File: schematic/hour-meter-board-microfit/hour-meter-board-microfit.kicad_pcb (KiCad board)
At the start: 2 copper layers, 80 x 92 mm, 143 parts, among them J101 VIN 9-30V, J201 USB-C, J301 DIN1 DIN2 COM, J501 WP, J701 RS485, J702 TERM, J703 BIAS, J801 UART, J802 GPS, J803 QWIIC, J804 EXP, J902 5V AIN1 GND DOUT1 GND, Q201 MMBT3904, Q202 MMBT3904, SW201 RESET, SW202 BOOT, U101 LM2596S-ADJ, U201 ESP32-WROOM-32E-N4, U202 CH340C, U203 USBLC6-2SC6, U204 AMS1117-3.3, U301 PC817C-S, U302 PC817C-S, U401 DS3231MZ+TRL, U501 AT24C256 DIP-8 (socketed), U601 MPU-6500, U602 LIS3MDLTR, U701 THVD2410DR, U801 74LVC1G17GW, U802 SRV05-4, U901 ADS1115IDGST, U902 SN74AHCT1G125DBVR, U903 BSP75N

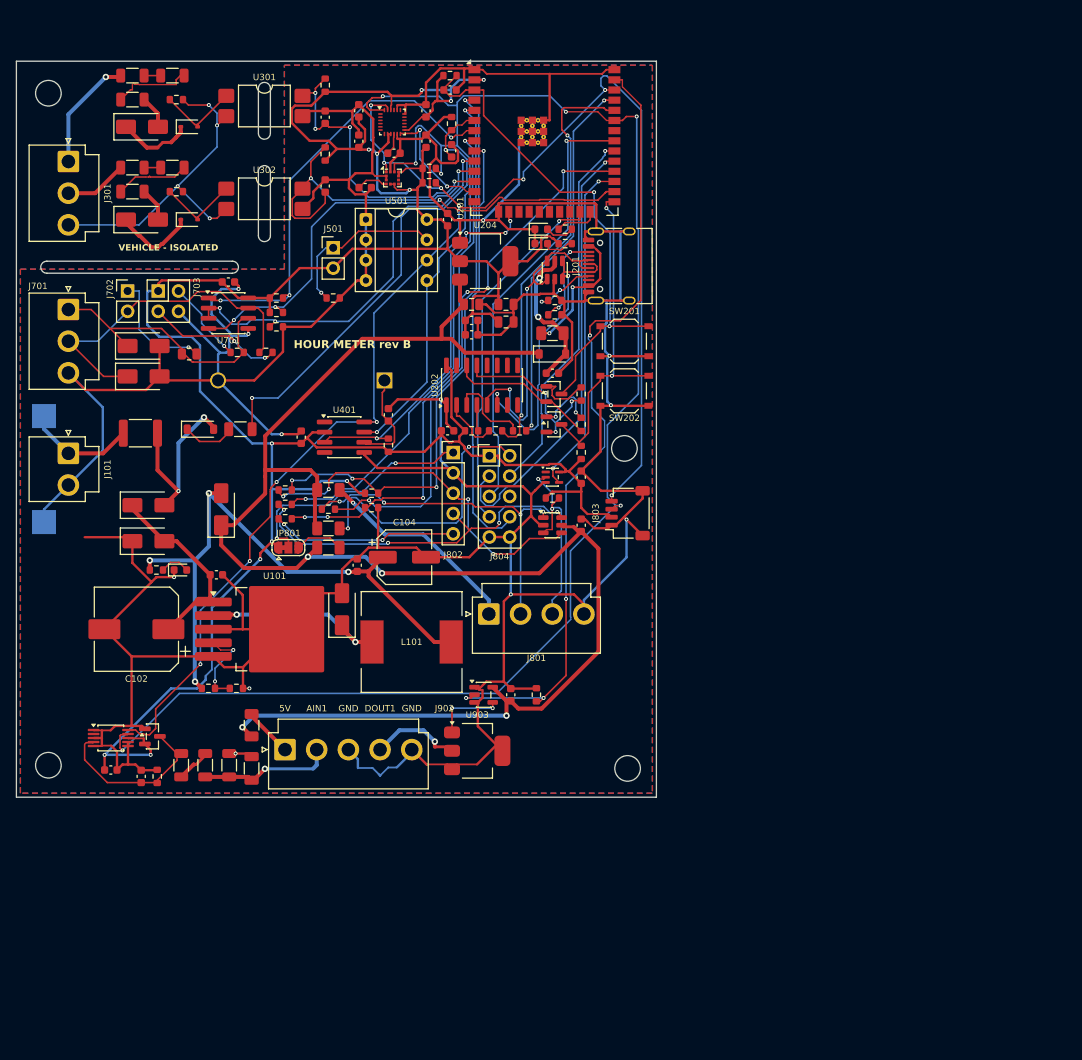
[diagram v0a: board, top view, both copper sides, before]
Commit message: feat(pcb): lay out the Micro-Fit harness board on 80 x 80 mm
- Every port on the left edge: J1 (Micro-Fit 2x7, mating face at the
  edge), the GPS JST GH port and the Qwiic port below it; USB-C and the
  buttons stay on the right edge.
- Vehicle zone beside J1: the DIN island in the top-left corner (slots,
  barrier rule areas, no pour; the GND pour keeps 3.65 mm away), then the
  RS485, UART, AIN1 and DOUT1 front ends, with the BSP75N's drain facing
  J1 so the 0.5 A loop stays at the connector. The LM2596 stage keeps
  its bottom strip; the coin cell moves to the bottom-right corner.
- The ESP32/USB block, the IMU and the LM2596 stage keep the I/O board's
  placement, and `reuse` copies their routing; KiCad's DRC drops any
  copied piece that clashes with the new layout. Freerouting routed the
  rest: DRC 0 errors, 0 unconnected, 0 parity, 2 copper layers.
- `silk` re-applies the labels on the routed board: a legend for the
  RS485 solder jumpers and the J1 pinout on the bottom silkscreen.
- J1's 3D model is JLCPCB's (C277677), fitted to the KiCad footprint.
- Order files: BOM 68 lines, CPL 125; all in stock for 10 boards.
- README: harness pinout and parts, ports, solder jumpers, enclosure.
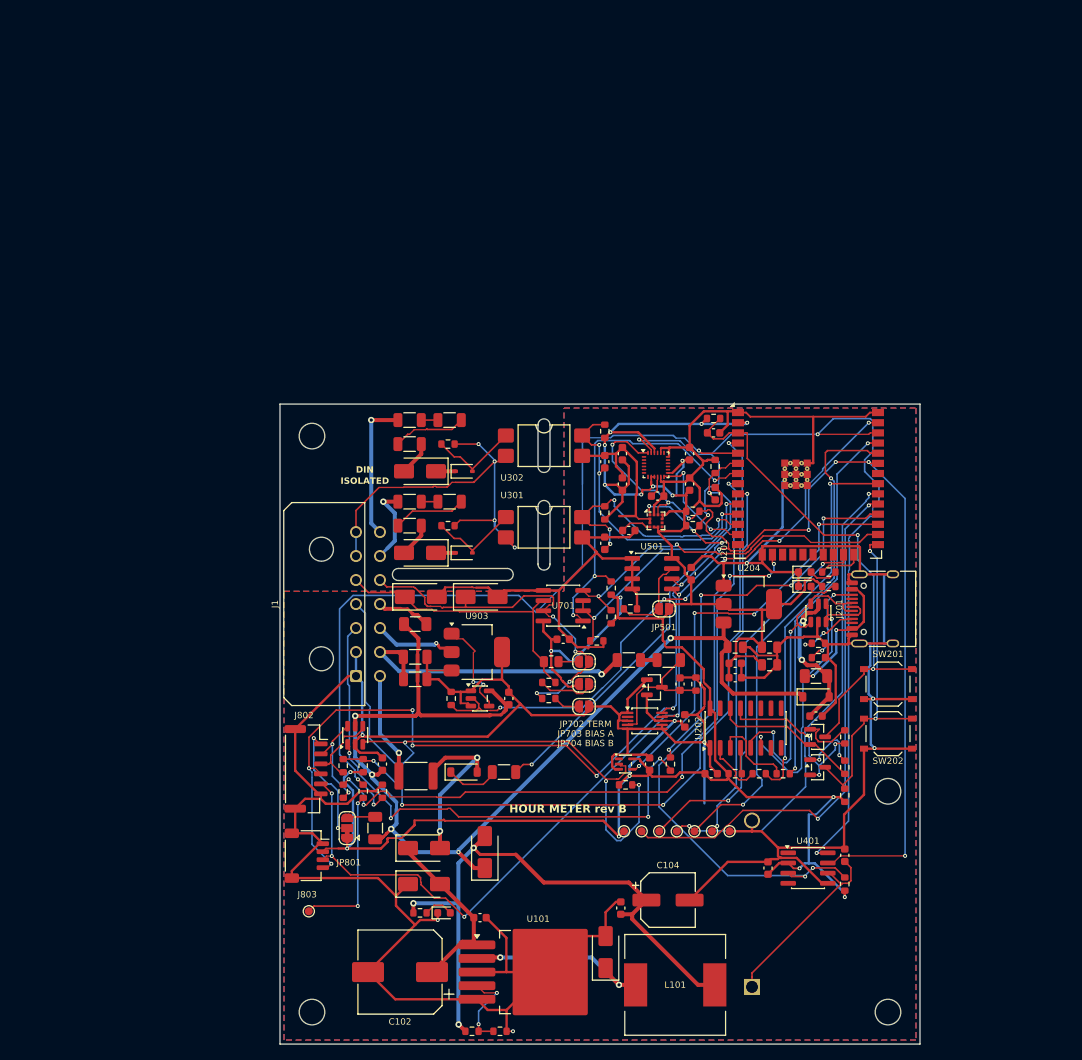
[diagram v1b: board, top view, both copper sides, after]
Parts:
- removed F802, F902: 0.2A, Fuse:Fuse_1206_3216Metric
- removed J101: VIN 9-30V, Connector_JST:JST_VH_B2P-VH_1x02_P3.96mm_Vertical
- removed J301: DIN1 DIN2 COM, Connector_JST:JST_VH_B3P-VH_1x03_P3.96mm_Vertical
- removed J501: WP, Connector_PinHeader_2.54mm:PinHeader_1x02_P2.54mm_Vertical
- removed J701: RS485, Connector_JST:JST_VH_B3P-VH_1x03_P3.96mm_Vertical
- removed J702: TERM, Connector_PinHeader_2.54mm:PinHeader_1x02_P2.54mm_Vertical
- removed J703: BIAS, Connector_PinHeader_2.54mm:PinHeader_2x02_P2.54mm_Vertical
- removed J801: UART, Connector_JST:JST_VH_B4P-VH_1x04_P3.96mm_Vertical
- removed J804: EXP, Connector_PinHeader_2.54mm:PinHeader_2x05_P2.54mm_Vertical
- removed J902: 5V AIN1 GND DOUT1 GND, Connector_JST:JST_VH_B5P-VH_1x05_P3.96mm_Vertical
- removed TP101: VIN, TestPoint:TestPoint_Pad_3.0x3.0mm
- removed TP102: GND, TestPoint:TestPoint_Pad_3.0x3.0mm
- added J1: Micro-Fit 3.0 2x7, Connector_Molex:Molex_Micro-Fit_3.0_43045-1400_2x07_P3.00mm_Horizontal, F.Cu at (109.5, 134.0)
- added JP501: WP, Jumper:SolderJumper-2_P1.3mm_Open_RoundedPad1.0x1.5mm, F.Cu at (148.0, 125.6)
- added JP702: TERM 120R, Jumper:SolderJumper-2_P1.3mm_Open_RoundedPad1.0x1.5mm, F.Cu at (138.0, 132.2)
- added JP703: BIAS A, Jumper:SolderJumper-2_P1.3mm_Open_RoundedPad1.0x1.5mm, F.Cu at (138.0, 135.0)
- added JP704: BIAS B, Jumper:SolderJumper-2_P1.3mm_Open_RoundedPad1.0x1.5mm, F.Cu at (138.0, 137.8)
- added TP801: PPS, TestPoint:TestPoint_Pad_D1.0mm, F.Cu at (103.6, 163.4)
- added TP802: IO5, TestPoint:TestPoint_Pad_D1.0mm, F.Cu at (145.2, 153.4)
- added TP803: IO15, TestPoint:TestPoint_Pad_D1.0mm, F.Cu at (147.4, 153.4)
- added TP804: IO18, TestPoint:TestPoint_Pad_D1.0mm, F.Cu at (149.6, 153.4)
- added TP805: IO19, TestPoint:TestPoint_Pad_D1.0mm, F.Cu at (151.8, 153.4)
- added TP806: IO33, TestPoint:TestPoint_Pad_D1.0mm, F.Cu at (154.0, 153.4)
- added TP807: +3V3, TestPoint:TestPoint_Pad_D1.0mm, F.Cu at (143.0, 153.4)
- added TP808: GND, TestPoint:TestPoint_Pad_D1.0mm, F.Cu at (156.2, 153.4)
- J802: value GPS -> GPS (GH 6-pin); footprint Connector_PinHeader_2.54mm:PinHeader_1x05_P2.54mm_Vertical -> Connector_JST:JST_GH_SM06B-GHS-TB_1x06-1MP_P1.25mm_Horizontal
- U501: value AT24C256 DIP-8 (socketed) -> AT24C256C-SSHL-T; footprint Package_DIP:DIP-8_W7.62mm_Socket -> Package_SO:SOIC-8_3.9x4.9mm_P1.27mm
- moved BT401 88.6 mm to (159.0, 172.9), turned to 90 degrees
- moved C401 79.4 mm to (161.0, 158.0)
- moved C402 79.3 mm to (170.6, 156.4)
- moved R401 79.1 mm to (170.6, 160.0)
- moved U401 79.1 mm to (166.0, 158.0)
- moved C903 72.0 mm to (150.6, 139.6), turned to 90 degrees
- moved C902 68.3 mm to (150.0, 135.0)
- moved R903 68.3 mm to (152.0, 135.0)
- moved U901 66.8 mm to (145.6, 139.6)
- moved R305 63.9 mm to (140.6, 113.6)
- moved C301 63.7 mm to (140.6, 117.4)
- moved D301 63.6 mm to (117.5, 118.6), turned to 180 degrees
- moved R301 63.5 mm to (116.2, 112.2)
- moved R302 63.5 mm to (121.2, 112.2)
- moved R303 63.5 mm to (116.2, 115.2)
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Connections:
- net /IO (AIN1, DOUT1)/AIN1_RAW renamed /AIN1_RAW
- net /Opto inputs (817 module 2ch)/VEH_GND renamed /VEH_GND
- net /Ports (UART, GPS, Qwiic, expansion)/UART_RXD_EXT renamed /UART_RXD_EXT
- net /Ports (UART, GPS, Qwiic, expansion)/UART_TXD_EXT renamed /UART_TXD_EXT
- net /RS485 (MAX485 module)/RS485_A renamed /RS485_A
- net /RS485 (MAX485 module)/RS485_B renamed /RS485_B
- F101 pad 1: Net-(J101-Pin_1) -> /VIN_IN
- F801 pad 2: /Ports (UART, GPS, Qwiic, expansion)/UART_5V -> /UART_5V
- J802 pad 2: GND -> /Ports (UART, GPS, Qwiic, expansion)/GPS_RX_EXT
- J802 pad 4: /Ports (UART, GPS, Qwiic, expansion)/GPS_RX_EXT -> /I2C_SCL
- J802 pad 5: /Ports (UART, GPS, Qwiic, expansion)/GPS_PPS_EXT -> /I2C_SDA
- R301 pad 1: /Opto inputs (817 module 2ch)/DIN1_RAW -> /DIN1_RAW
- R306 pad 1: /Opto inputs (817 module 2ch)/DIN2_RAW -> /DIN2_RAW
- U903 pad 2: /IO (AIN1, DOUT1)/DOUT1 -> /DOUT1
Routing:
- net GND: track 706.9 -> 630.5 mm, vias 12 -> 7
- net +5V: track 203.7 -> 134.0 mm, vias 4 -> 5
- net /UART_RXD_EXT: track 25.9 -> 81.3 mm, vias 2 -> 3
- net /Ports (UART, GPS, Qwiic, expansion)/EXP_5V: track 35.2 -> 0.00 mm, vias 2 -> 0
- net /Ports (UART, GPS, Qwiic, expansion)/GPS_TX_EXT: track 45.3 -> 10.5 mm, vias 4 -> 0
- net /Ports (UART, GPS, Qwiic, expansion)/GPS_RX_EXT: track 45.9 -> 12.8 mm, vias 4 -> 2
- net /I2C_SCL: track 199.3 -> 229.5 mm, vias 11 -> 14
- net /GPS_PPS: track 70.6 -> 99.1 mm, vias 4 -> 3
- net /GPS_RXD: track 59.8 -> 88.0 mm, vias 2 -> 4
- net /UART_TXD_EXT: track 43.2 -> 70.7 mm
- net /Ports (UART, GPS, Qwiic, expansion)/UART_5V: track 26.1 -> 0.00 mm, vias 1 -> 0
- net /I2C_SDA: track 241.9 -> 215.8 mm, vias 8 -> 13
- net /DOUT1_CTRL: track 99.8 -> 74.8 mm, vias 4 -> 6
- net +3V3: track 354.7 -> 330.9 mm, vias 12 -> 19
- net /RTC_INT: track 46.8 -> 70.5 mm, vias 4 -> 5
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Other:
- board size 80 x 92 mm -> 80 x 80 mm
- board text added: "1 GND 8 VIN"
- board text added: "2 GND 9 AIN1"
- board text added: "3 TX 10 DOUT1"
- board text added: "4 RX 11 +5V"
- board text added: "5 485 A 12 485 B"
- board text added: "6 DIN COM 13 DIN1"
- board text added: "7 DIN COM 14 DIN2"
- board text added: "DIN"
- board text added: "ISOLATED"
- board text added: "J1 MICRO-FIT 3.0"
- board text added: "JP702 TERM"
- board text added: "JP703 BIAS A"
- board text added: "JP704 BIAS B"
- board text removed: "5V"
- board text removed: "AIN1"
- board text removed: "DOUT1"
- board text removed: "GND"
- board text removed: "VEHICLE - ISOLATED"

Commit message: feat(pcb): add three side-view indicator LEDs to the Micro-Fit board
- D801 P1 (green, GPIO18) and D802 P2 (yellow, GPIO19) are process
  indicators; D803 USER (blue, GPIO5) is free for the program. They are
  Lite-On LTST-S270 side-view LEDs on the right edge below H103, lenses
  at the board edge, 330R each, active high. GPIO5/18/19 were the test
  pads TP802/TP804/TP805.
- tools-pcb.py: `update` adds and removes parts on the routed board;
  `route`, `finish`, `update` and `silk` follow a board moved in KiCad
  (offset measured on U601); add_pinout draws the two-column J1 pinout.
- Keeps the KiCad edits made after the layout commit: the board moved
  by (18.20, -48.27) mm and the bottom-silkscreen pinout split into two
  columns.
- DRC 0 errors, 0 unconnected, 0 parity; BOM 71 lines, CPL 131, all in
  stock for 10 boards.
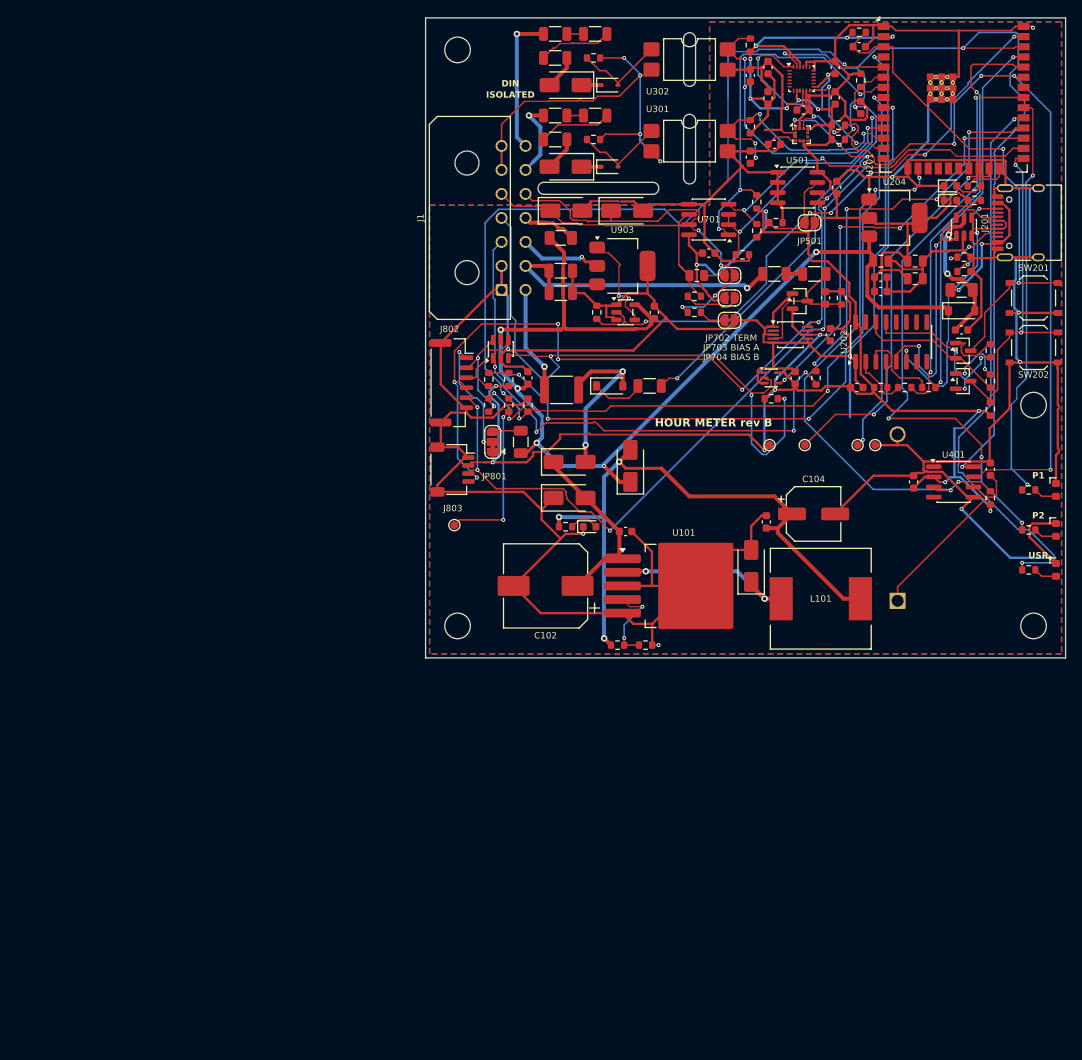
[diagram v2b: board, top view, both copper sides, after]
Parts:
- removed TP802: IO5, TestPoint:TestPoint_Pad_D1.0mm
- removed TP804: IO18, TestPoint:TestPoint_Pad_D1.0mm
- removed TP805: IO19, TestPoint:TestPoint_Pad_D1.0mm
- added D801: P1 (green), LED_SMD:LED_Kingbright_APA1606_1.6x0.6mm_Horizontal, F.Cu at (197.0, 110.7)
- added D802: P2 (yellow), LED_SMD:LED_Kingbright_APA1606_1.6x0.6mm_Horizontal, F.Cu at (197.0, 115.7)
- added D803: USER (blue), LED_SMD:LED_Kingbright_APA1606_1.6x0.6mm_Horizontal, F.Cu at (197.0, 120.7)
- added R808: 330R, Resistor_SMD:R_0603_1608Metric, F.Cu at (193.6, 110.7)
- added R809: 330R, Resistor_SMD:R_0603_1608Metric, F.Cu at (193.6, 115.7)
- added R810: 330R, Resistor_SMD:R_0603_1608Metric, F.Cu at (193.6, 120.7)
- moved R103 51.6 mm to (142.2, 130.1)
- moved R104 51.6 mm to (145.7, 130.1)
- moved BT401 51.6 mm to (177.2, 124.6)
- moved C101 51.6 mm to (172.6, 62.9)
- moved C102 51.6 mm to (133.2, 122.7)
- moved C104 51.6 mm to (166.7, 113.7)
- moved C105 51.6 mm to (160.8, 114.7)
- moved C201 51.6 mm to (179.4, 82.1)
- moved C202 51.6 mm to (175.1, 84.1)
- moved C205 51.6 mm to (175.1, 82.1)
- moved C208 51.6 mm to (185.2, 90.7)
- moved C301 51.6 mm to (158.8, 69.1)
- moved C302 51.6 mm to (158.8, 58.9)
- moved C401 51.6 mm to (179.2, 109.7)
- moved C402 51.6 mm to (188.8, 108.1)
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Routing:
- net GND: track 630.5 -> 679.5 mm, vias 7 -> 10
- net /EXP_IO19: track 58.8 -> 77.0 mm, vias 2 -> 4
- net /EXP_IO18: track 60.0 -> 51.1 mm
- net /EXP_IO5: track 67.3 -> 70.3 mm
- net /VEH_GND: track 53.2 -> 56.2 mm
- net Net-(D803-A): track 0.00 -> 2.91 mm
- net Net-(D802-A): track 0.00 -> 2.91 mm
- net Net-(D801-A): track 0.00 -> 2.91 mm
- net /RS485_A: track 35.9 -> 37.8 mm
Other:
- outline, holes or cut-outs redrawn
- board text added: "1 GND"
- board text added: "10 DOUT1"
- board text added: "11 +5V"
- board text added: "12 485 B"
- board text added: "13 DIN1"
- board text added: "14 DIN2"
- board text added: "2 GND"
- board text added: "3 TX"
- board text added: "4 RX"
- board text added: "5 485 A"
- board text added: "6 DIN COM"
- board text added: "7 DIN COM"
- board text added: "8 VIN"
- board text added: "9 AIN1"
- board text added: "P1"
- board text added: "P2"
- board text added: "USR"
- board text removed: "1 GND 8 VIN"
- board text removed: "2 GND 9 AIN1"
- board text removed: "3 TX 10 DOUT1"
- board text removed: "4 RX 11 +5V"
- board text removed: "5 485 A 12 485 B"
- board text removed: "6 DIN COM 13 DIN1"
- board text removed: "7 DIN COM 14 DIN2"

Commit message: feat(pcb): one green LED part and a pinout spec for the Micro-Fit board
D802 and D803 become the green LTST-S270TGKT, like D801. Its JLCPCB
model faces the board edge like the KiCad footprint, where the yellow
and blue parts' models faced the other way, and one LED part means two
fewer extended parts. `update` now also brings the value and fields of
parts that stay in line with the schematic.

PINOUT.md gives every J1 pin's working range, absolute maximum and
current, the other ports, the I2C addresses in use, and the power
budget at 12 V: 0.5 W idle, 0.8 W typical, about 4 W with every port
at its limit. The trucks feed the board from a 24 -> 12 V converter.
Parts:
- D802: value P2 (yellow) -> P2 (green)
- D803: value USER (blue) -> USER (green)
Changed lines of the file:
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@@
 			)
 		)
-		(property "Value" "USER (blue)"
+		(property "Value" "USER (green)"
 			(at 0 1.6 270)
 			(layer "F.Fab")
@@
 			)
 		)
-		(property "Description" "Side-view LED, blue, 1.6 x 1.2 mm (Lite-On LTST-S270); lights out of the right board edge"
+		(property "Description" "Side-view LED, green, 1.6 x 1.2 mm (Lite-On LTST-S270); lights out of the right board edge"
 			(at 0 0 270)
 			(unlocked yes)
@@
 			)
 		)
-		(property "LCSC" "C125115"
+		(property "LCSC" "C364567"
 			(at 0 0 270)
 			(layer "F.SilkS")
@@
 			)
 		)
-		(property "MPN" "LTST-S270TBKT"
+		(property "MPN" "LTST-S270TGKT"
 			(at 0 0 270)
 			(layer "F.SilkS")
@@
 			)
 		)
-		(property "Value" "P2 (yellow)"
+		(property "Value" "P2 (green)"
 			(at 0 1.6 270)
 			(layer "F.Fab")
@@
 			)
 		)
-		(property "Description" "Side-view LED, yellow, 1.6 x 1.2 mm (Lite-On LTST-S270); lights out of the right board edge"
+		(property "Description" "Side-view LED, green, 1.6 x 1.2 mm (Lite-On LTST-S270); lights out of the right board edge"
 			(at 0 0 270)
 			(unlocked yes)
@@
 			)
 		)
-		(property "LCSC" "C133119"
+		(property "LCSC" "C364567"
 			(at 0 0 270)
 			(layer "F.SilkS")
@@
 			)
 		)
-		(property "MPN" "LTST-S270KSKT"
+		(property "MPN" "LTST-S270TGKT"
 			(at 0 0 270)
 			(layer "F.SilkS")
